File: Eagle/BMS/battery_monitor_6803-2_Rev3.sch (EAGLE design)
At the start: 66 parts, among them Q1 MOSFET-PCHANNELIRLML2244, Q10 IRF9530, Q2 MOSFET-NCHANNELBSS138, Q3 MOSFET-PCHANNELIRLML2244, Q4 MOSFET-PCHANNELIRLML2244, Q5 MOSFET-PCHANNELIRLML2244, Q6 MOSFET-NCHANNELBSS138, Q7 MOSFET-NCHANNELBSS138, Q8 MOSFET-NCHANNELBSS138, Q9 PMOS_AO4435

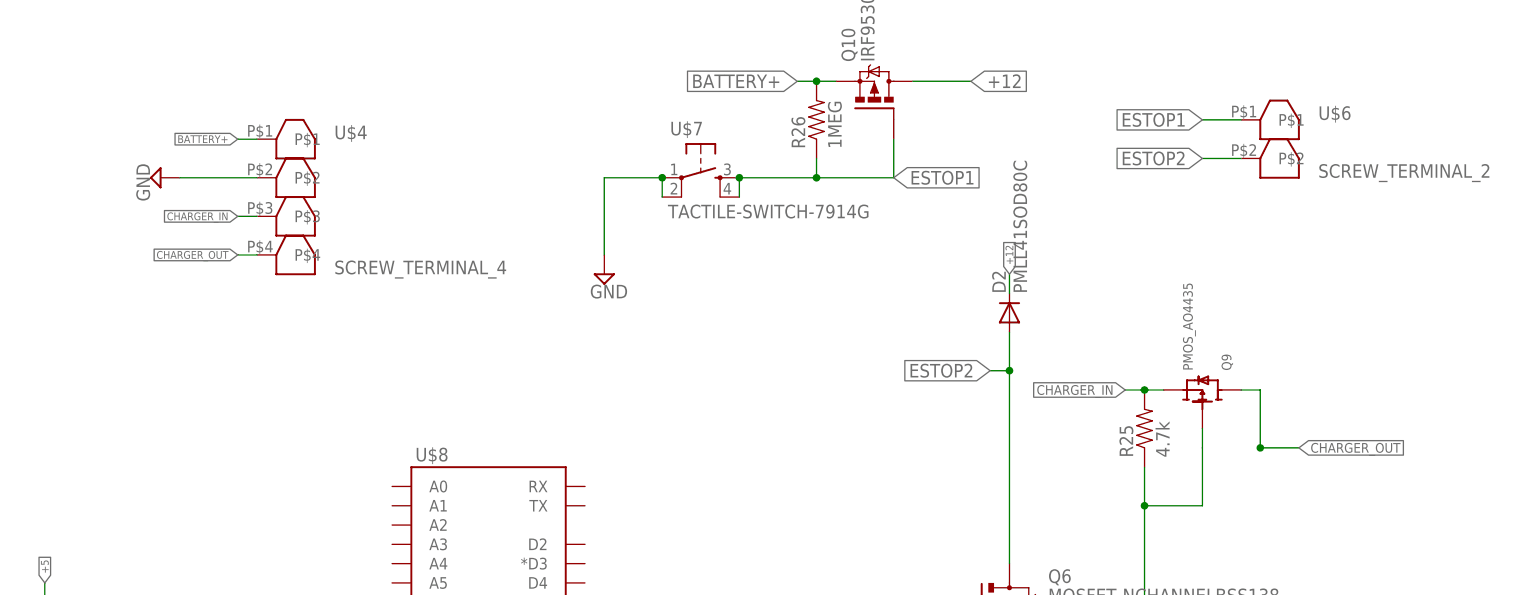
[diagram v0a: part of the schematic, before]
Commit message: Encoder design Rev1 changes.
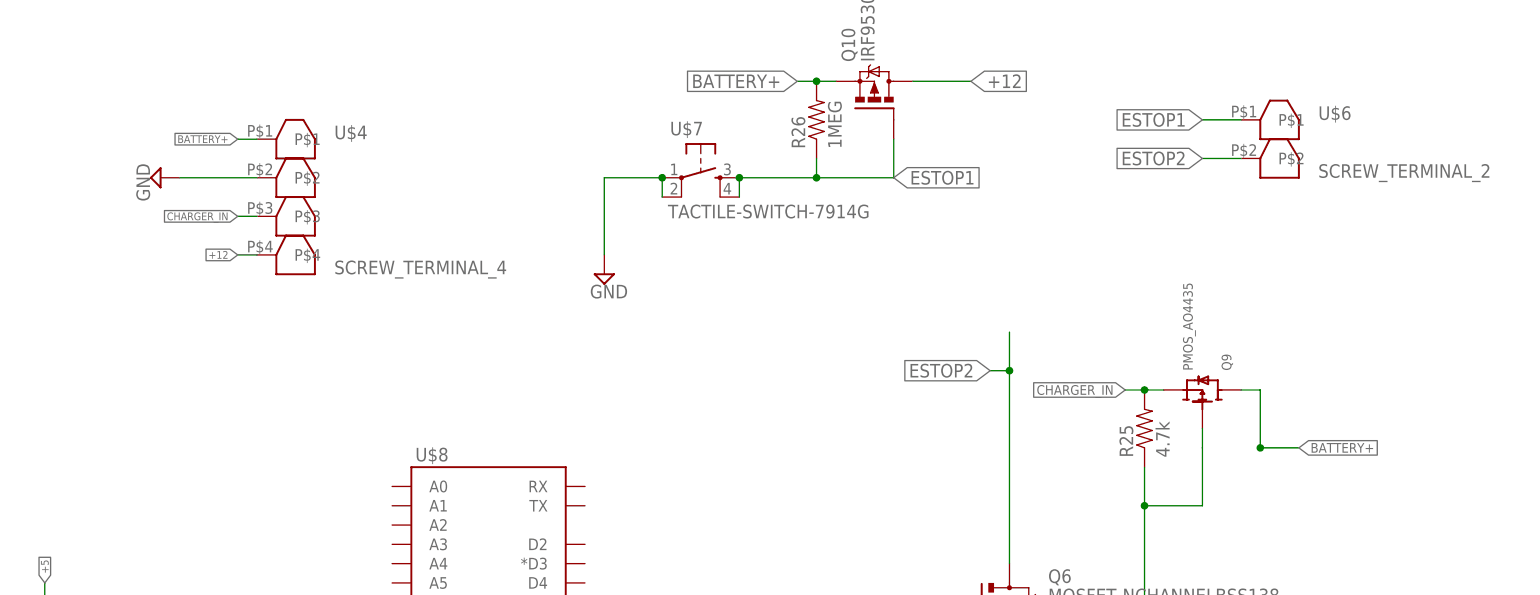
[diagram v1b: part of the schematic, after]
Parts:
- removed D2: PMLL41SOD80C, diode:PMLL41SOD80C
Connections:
- removed net CHARGER_OUT: Q9.DRAIN, U$4.P$4
- net +12: now also U$4.P$4; no longer D2.C
- net BATTERY+: now also Q9.DRAIN
- net ESTOP2: no longer D2.A
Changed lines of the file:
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@@
 <part name="SUPPLY10" library="supply2" deviceset="GND" device=""/>
 <part name="SUPPLY11" library="supply2" deviceset="GND" device=""/>
-<part name="D2" library="diode" deviceset="PMLL41*" device="SOD80C">
-<attribute name="MF" value="FAIRCHILD SEMICONDUCTOR"/>
-<attribute name="MPN" value="FDLL4148"/>
-<attribute name="OC_NEWARK" value="18C6408"/>
-</part>
 <part name="I2C" library="isaac1" deviceset="SCREW_TERMINAL_2" device="">
 <attribute name="MF" value="TYCO ELECTRONICS"/>
@@
 <instance part="SUPPLY10" gate="GND" x="231.14" y="-2.54"/>
 <instance part="SUPPLY11" gate="GND" x="210.82" y="10.16"/>
-<instance part="D2" gate="G$1" x="223.52" y="60.96" rot="R90">
-<attribute name="OC_NEWARK" x="223.52" y="60.96" size="1.778" layer="96" display="off"/>
-<attribute name="MF" x="223.52" y="60.96" size="1.778" layer="96" display="off"/>
-<attribute name="MPN" x="223.52" y="60.96" size="1.778" layer="96" display="off"/>
-</instance>
 <instance part="I2C" gate="G$1" x="205.74" y="0">
 <attribute name="OC_NEWARK" x="205.74" y="0" size="1.778" layer="96" display="off"/>
@@
 </segment>
 <segment>
-<pinref part="D2" gate="G$1" pin="C"/>
-<wire x1="223.52" y1="63.5" x2="223.52" y2="66.04" width="0.1524" layer="91"/>
-<label x="223.52" y="66.04" size="1.016" layer="95" rot="R90" xref="yes"/>
-</segment>
-<segment>
 <pinref part="Q10" gate="G$1" pin="D"/>
 <wire x1="210.82" y1="91.44" x2="218.44" y2="91.44" width="0.1524" layer="91"/>
 <label x="218.44" y="91.44" size="1.778" layer="95" xref="yes"/>
+</segment>
+<segment>
+<pinref part="U$4" gate="G$1" pin="P$4"/>
+<wire x1="124.46" y1="68.58" x2="121.92" y2="68.58" width="0.1524" layer="91"/>
+<label x="121.92" y="68.58" size="1.016" layer="95" rot="R180" xref="yes"/>
 </segment>
 </net>
@@
 </segment>
 </net>
-<net name="CHARGER_OUT" class="0">
+<net name="ESTOP2" class="0">
+<segment>
+<pinref part="U$6" gate="G$1" pin="P$2"/>
+<wire x1="254" y1="81.28" x2="248.92" y2="81.28" width="0.1524" layer="91"/>
+<label x="248.92" y="81.28" size="1.778" layer="95" rot="R180" xref="yes"/>
+</segment>
+<segment>
+<pinref part="Q6" gate="G$1" pin="D"/>
+<wire x1="223.52" y1="58.42" x2="223.52" y2="53.34" width="0.1524" layer="91"/>
+<wire x1="223.52" y1="53.34" x2="223.52" y2="27.94" width="0.1524" layer="91"/>
+<wire x1="223.52" y1="53.34" x2="220.98" y2="53.34" width="0.1524" layer="91"/>
+<junction x="223.52" y="53.34"/>
+<label x="220.98" y="53.34" size="1.778" layer="95" rot="R180" xref="yes"/>
+</segment>
+</net>
+<net name="BATTERY+" class="0">
+<segment>
+<pinref part="Q10" gate="G$1" pin="S"/>
+<wire x1="200.66" y1="91.44" x2="198.12" y2="91.44" width="0.1524" layer="91"/>
+<wire x1="198.12" y1="91.44" x2="195.58" y2="91.44" width="0.1524" layer="91"/>
+<junction x="198.12" y="91.44"/>
+<label x="195.58" y="91.44" size="1.778" layer="95" rot="R180" xref="yes"/>
+<pinref part="R26" gate="G$1" pin="2"/>
+</segment>
+<segment>
+<wire x1="124.46" y1="83.82" x2="121.92" y2="83.82" width="0.1524" layer="91"/>
+<label x="121.92" y="83.82" size="1.016" layer="95" rot="R180" xref="yes"/>
+<pinref part="U$4" gate="G$1" pin="P$1"/>
+</segment>
 <segment>
 <wire x1="256.54" y1="43.18" x2="261.62" y2="43.18" width="0.1524" layer="91"/>
@@
 <junction x="256.54" y="43.18"/>
 </segment>
-<segment>
-<pinref part="U$4" gate="G$1" pin="P$4"/>
-<wire x1="124.46" y1="68.58" x2="121.92" y2="68.58" width="0.1524" layer="91"/>
-<label x="121.92" y="68.58" size="1.016" layer="95" rot="R180" xref="yes"/>
-</segment>
-</net>
-<net name="ESTOP2" class="0">
-<segment>
-<pinref part="U$6" gate="G$1" pin="P$2"/>
-<wire x1="254" y1="81.28" x2="248.92" y2="81.28" width="0.1524" layer="91"/>
-<label x="248.92" y="81.28" size="1.778" layer="95" rot="R180" xref="yes"/>
-</segment>
-<segment>
-<pinref part="D2" gate="G$1" pin="A"/>
-<pinref part="Q6" gate="G$1" pin="D"/>
-<wire x1="223.52" y1="58.42" x2="223.52" y2="53.34" width="0.1524" layer="91"/>
-<wire x1="223.52" y1="53.34" x2="223.52" y2="27.94" width="0.1524" layer="91"/>
-<wire x1="223.52" y1="53.34" x2="220.98" y2="53.34" width="0.1524" layer="91"/>
-<junction x="223.52" y="53.34"/>
-<label x="220.98" y="53.34" size="1.778" layer="95" rot="R180" xref="yes"/>
-</segment>
-</net>
-<net name="BATTERY+" class="0">
-<segment>
-<pinref part="Q10" gate="G$1" pin="S"/>
-<wire x1="200.66" y1="91.44" x2="198.12" y2="91.44" width="0.1524" layer="91"/>
-<wire x1="198.12" y1="91.44" x2="195.58" y2="91.44" width="0.1524" layer="91"/>
-<junction x="198.12" y="91.44"/>
-<label x="195.58" y="91.44" size="1.778" layer="95" rot="R180" xref="yes"/>
-<pinref part="R26" gate="G$1" pin="2"/>
-</segment>
-<segment>
-<wire x1="124.46" y1="83.82" x2="121.92" y2="83.82" width="0.1524" layer="91"/>
-<label x="121.92" y="83.82" size="1.016" layer="95" rot="R180" xref="yes"/>
-<pinref part="U$4" gate="G$1" pin="P$1"/>
-</segment>
-</net>
+</net>
